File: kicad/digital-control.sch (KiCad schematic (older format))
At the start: 25 parts, among them J3 CONN_01X04, SW1 JS5208, U4 STM32F031G, U5 SSD1306-OLED-I2C, U6 MMA8652FC

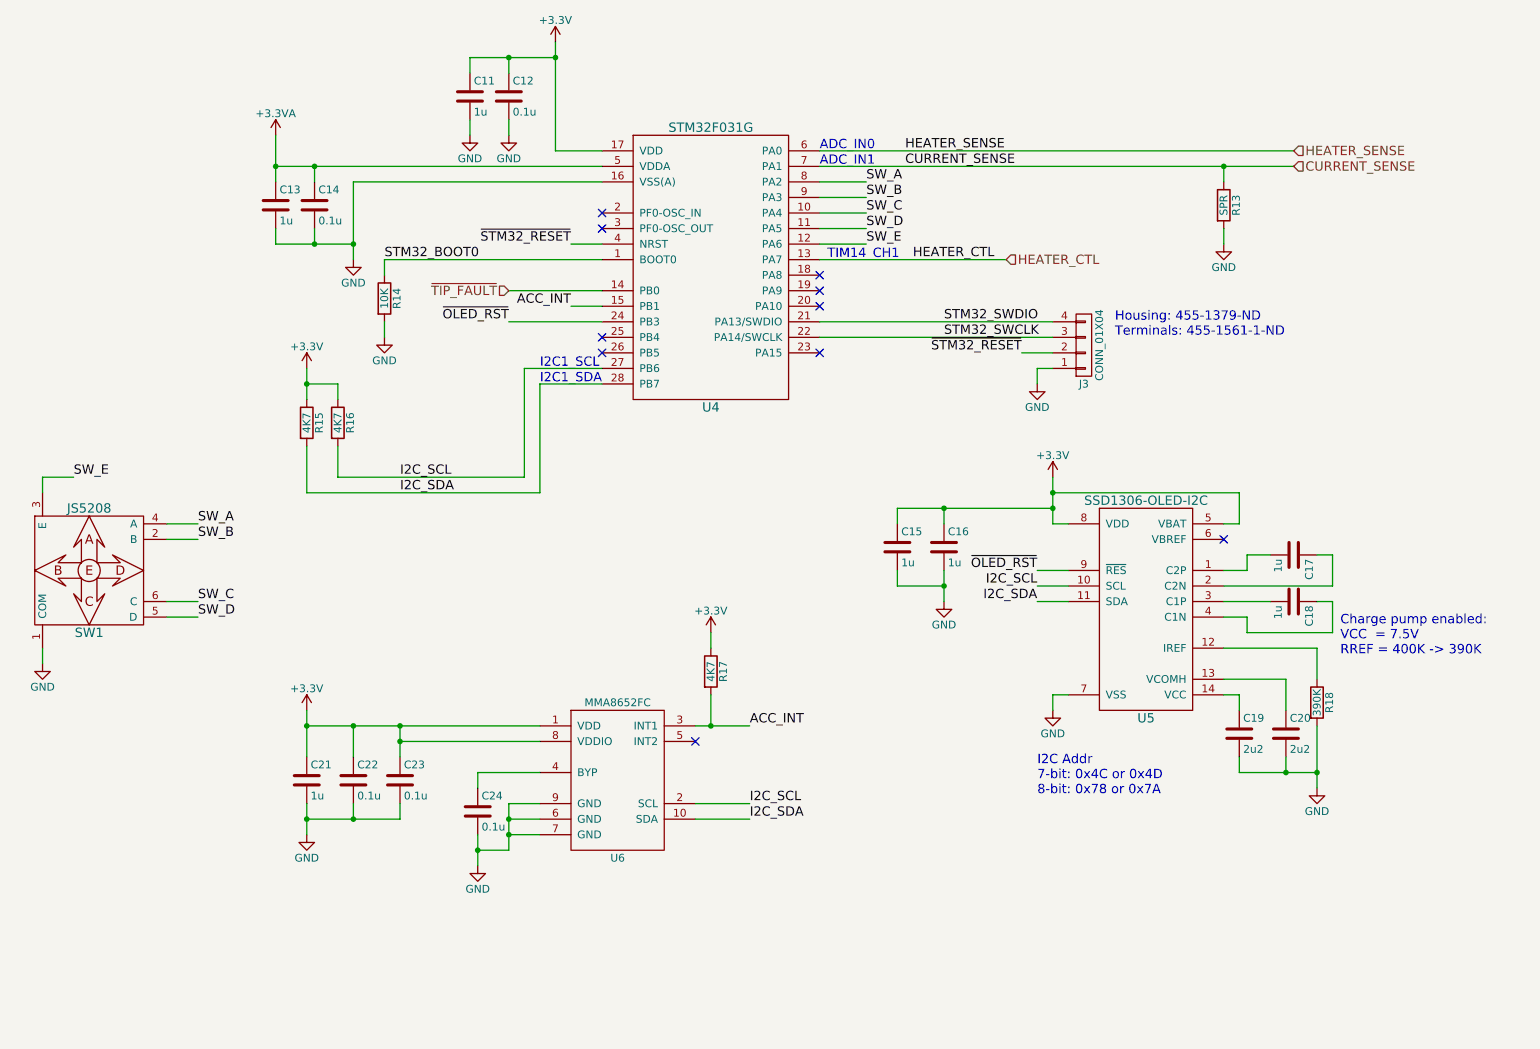
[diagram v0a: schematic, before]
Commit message: Added buzzer, fixed footprint errors, and updated silkscreen
The board is probably ready to be ordered
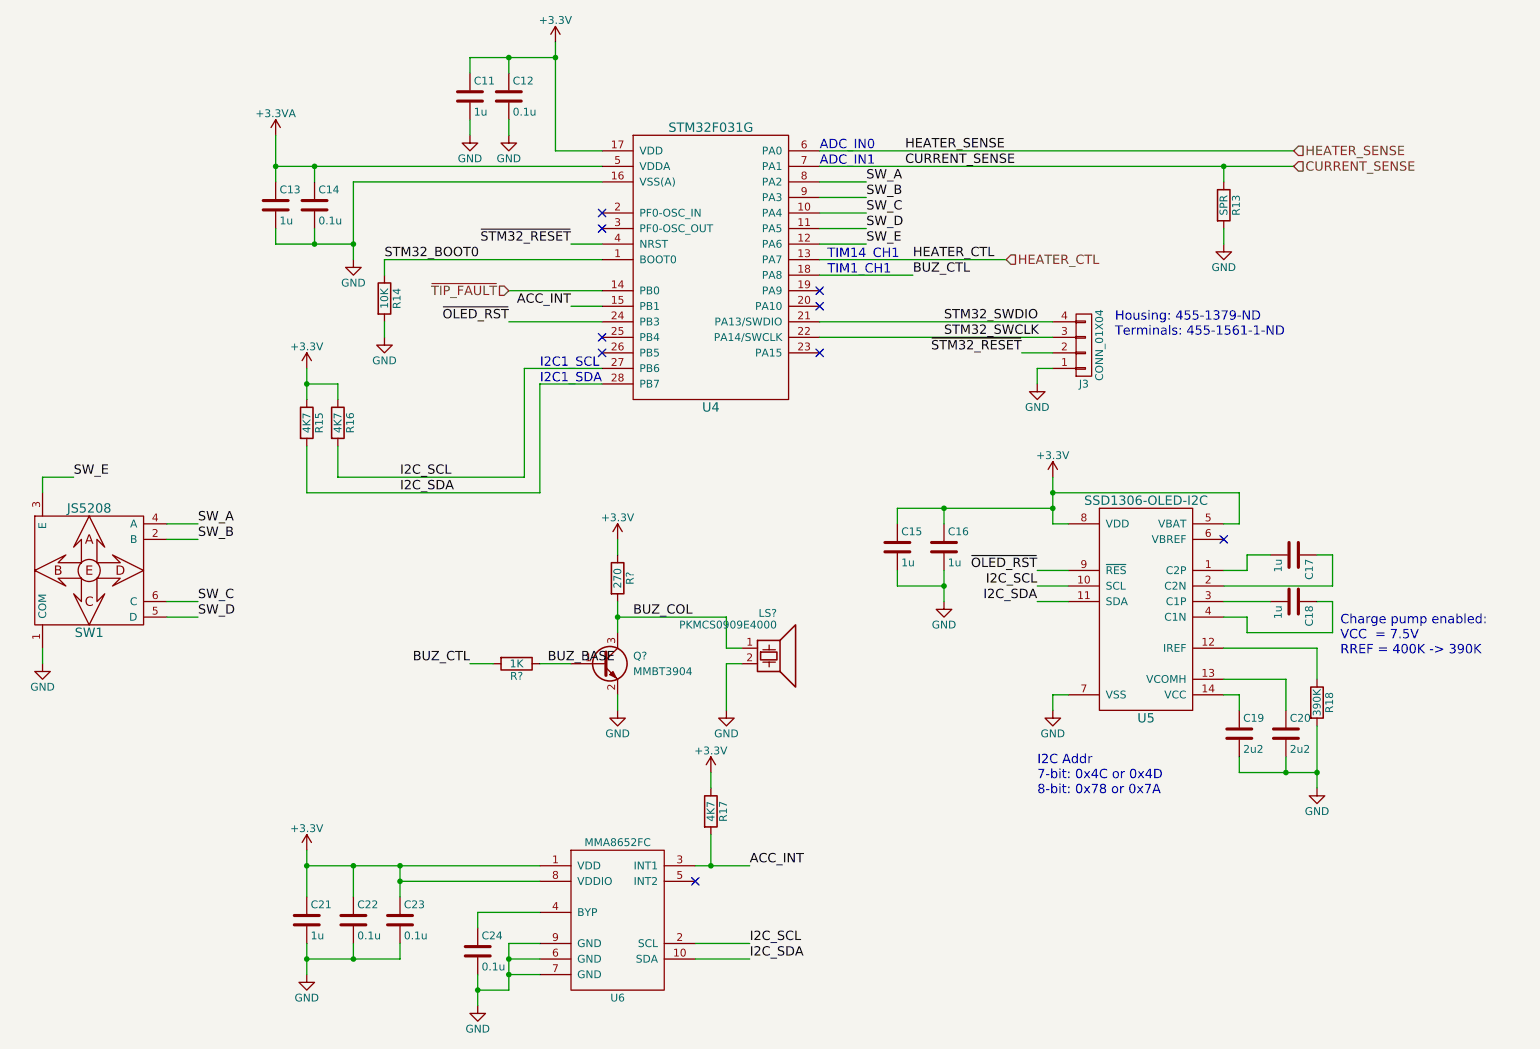
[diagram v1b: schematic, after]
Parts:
- added LS?: PKMCS0909E4000, rt-soldering-iron:Murata-PKMCS, symbol Speaker_Crystal
- added Q?: MMBT3904, TO_SOT_Packages_SMD:SOT-323_SC-70, symbol Q_NPN_BEC
- added R?: 270, Resistors_SMD:R_0402, symbol R
- added R?: 1K, Resistors_SMD:R_0402, symbol R
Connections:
- net +3V3: now also R?.1
- net GND: now also LS?.2, Q?.2 (E)
- net BUZ_CTL: now reaches U4.18 (PA8)
- net BUZ_CTL: now also R?.2
- new net BUZ_BASE: Q?.1 (B), R?.1
- new net BUZ_COL: LS?.1, Q?.3 (C), R?.2
- no-connect marks 10 -> 9
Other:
- note added: "TIM1_CH1"
- moved on the sheet: C21, C22, C23, C24, R17, U6

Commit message: Changed out the op amp and fixed oval holes for OSHPark
I don't think I'm going to go with OSHPark. It seems they can't
fabricate this thing.
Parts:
- gave numbers to parts that had none: 4
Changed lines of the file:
@@
 encoding utf-8
 Sheet 4 4
-Title ""
-Date ""
-Rev ""
-Comp ""
+Title "RT Soldering Iron"
+Date "2017-06-02"
+Rev "A"
+Comp "Kevin Cuzner"
 Comment1 ""
 Comment2 ""
@@
 $EndComp
 $Comp
-L +3.3V #PWR031
+L +3.3V #PWR33
 U 1 1 592BB6CC
 P 4600 1000
-F 0 "#PWR031" H 4600 850 50  0001 C CNN
+F 0 "#PWR33" H 4600 850 50  0001 C CNN
 F 1 "+3.3V" H 4600 1140 50  0000 C CNN
 F 2 "" H 4600 1000 50  0001 C CNN
@@
 $EndComp
 $Comp
-L GND #PWR032
+L GND #PWR38
 U 1 1 592BB766
 P 3300 2400
-F 0 "#PWR032" H 3300 2150 50  0001 C CNN
+F 0 "#PWR38" H 3300 2150 50  0001 C CNN
 F 1 "GND" H 3300 2250 50  0000 C CNN
 F 2 "" H 3300 2400 50  0001 C CNN
@@
 Connection ~ 4600 1100
 $Comp
-L GND #PWR033
+L GND #PWR36
 U 1 1 592BB8F3
 P 4300 1600
-F 0 "#PWR033" H 4300 1350 50  0001 C CNN
+F 0 "#PWR36" H 4300 1350 50  0001 C CNN
 F 1 "GND" H 4300 1450 50  0000 C CNN
 F 2 "" H 4300 1600 50  0001 C CNN
@@
 $EndComp
 $Comp
-L GND #PWR034
+L GND #PWR35
 U 1 1 592BB980
 P 4050 1600
-F 0 "#PWR034" H 4050 1350 50  0001 C CNN
+F 0 "#PWR35" H 4050 1350 50  0001 C CNN
 F 1 "GND" H 4050 1450 50  0000 C CNN
 F 2 "" H 4050 1600 50  0001 C CNN
@@
 	3500 2400 4900 2400
 $Comp
-L GND #PWR035
+L GND #PWR39
 U 1 1 592BBD79
 P 3500 2900
-F 0 "#PWR035" H 3500 2650 50  0001 C CNN
+F 0 "#PWR39" H 3500 2650 50  0001 C CNN
 F 1 "GND" H 3500 2750 50  0000 C CNN
 F 2 "" H 3500 2900 50  0001 C CNN
@@
 	2800 1800 4900 1800
 $Comp
-L +3.3VA #PWR036
+L +3.3VA #PWR34
 U 1 1 592C93D2
 P 2800 1600
-F 0 "#PWR036" H 2800 1450 50  0001 C CNN
+F 0 "#PWR34" H 2800 1450 50  0001 C CNN
 F 1 "+3.3VA" H 2800 1740 50  0000 C CNN
 F 2 "" H 2800 1600 50  0001 C CNN
@@
 	3000 3900 3000 3600
 $Comp
-L +3.3V #PWR037
+L +3.3V #PWR40
 U 1 1 592CB325
 P 3000 3100
-F 0 "#PWR037" H 3000 2950 50  0001 C CNN
+F 0 "#PWR40" H 3000 2950 50  0001 C CNN
 F 1 "+3.3V" H 3000 3240 50  0000 C CNN
 F 2 "" H 3000 3100 50  0001 C CNN
@@
 	7700 4600 7900 4600
 $Comp
-L GND #PWR038
+L GND #PWR48
 U 1 1 592CB60F
 P 7800 5300
-F 0 "#PWR038" H 7800 5050 50  0001 C CNN
+F 0 "#PWR48" H 7800 5050 50  0001 C CNN
 F 1 "GND" H 7800 5150 50  0000 C CNN
 F 2 "" H 7800 5300 50  0001 C CNN
@@
 Housing: 455-1379-ND\nTerminals: 455-1561-1-ND
 $Comp
-L +3.3V #PWR039
+L +3.3V #PWR42
 U 1 1 592CC5EE
 P 7800 3800
-F 0 "#PWR039" H 7800 3650 50  0001 C CNN
+F 0 "#PWR42" H 7800 3650 50  0001 C CNN
 F 1 "+3.3V" H 7800 3940 50  0000 C CNN
 F 2 "" H 7800 3800 50  0001 C CNN
@@
 	7800 4100 7900 4100
 $Comp
-L GND #PWR040
+L GND #PWR41
 U 1 1 592CC80A
 P 7700 3200
-F 0 "#PWR040" H 7700 2950 50  0001 C CNN
+F 0 "#PWR41" H 7700 2950 50  0001 C CNN
 F 1 "GND" H 7700 3050 50  0000 C CNN
 F 2 "" H 7700 3200 50  0001 C CNN
@@
 Connection ~ 3300 6300
 $Comp
-L GND #PWR041
+L GND #PWR52
 U 1 1 592CCD51
 P 3000 7000
-F 0 "#PWR041" H 3000 6750 50  0001 C CNN
+F 0 "#PWR52" H 3000 6750 50  0001 C CNN
 F 1 "GND" H 3000 6850 50  0000 C CNN
 F 2 "" H 3000 7000 50  0001 C CNN
@@
 $EndComp
 $Comp
-L +3.3V #PWR042
+L +3.3V #PWR51
 U 1 1 592CCDF7
 P 3000 6200
-F 0 "#PWR042" H 3000 6050 50  0001 C CNN
+F 0 "#PWR51" H 3000 6050 50  0001 C CNN
 F 1 "+3.3V" H 3000 6340 50  0000 C CNN
 F 2 "" H 3000 6200 50  0001 C CNN
@@
 	4100 6600 4100 6700
 $Comp
-L GND #PWR043
+L GND #PWR53
 U 1 1 592CD0B5
 P 4100 7200
-F 0 "#PWR043" H 4100 6950 50  0001 C CNN
+F 0 "#PWR53" H 4100 6950 50  0001 C CNN
 F 1 "GND" H 4100 7050 50  0000 C CNN
 F 2 "" H 4100 7200 50  0001 C CNN
@@
 	9500 4900 9500 5100
 $Comp
-L GND #PWR044
+L GND #PWR50
 U 1 1 592D0F0D
 P 9500 5800
-F 0 "#PWR044" H 9500 5550 50  0001 C CNN
+F 0 "#PWR50" H 9500 5550 50  0001 C CNN
 F 1 "GND" H 9500 5650 50  0000 C CNN
 F 2 "" H 9500 5800 50  0001 C CNN
@@
 Connection ~ 7100 4000
 $Comp
-L GND #PWR045
+L GND #PWR44
 U 1 1 592D28AB
 P 7100 4600
-F 0 "#PWR045" H 7100 4350 50  0001 C CNN
+F 0 "#PWR44" H 7100 4350 50  0001 C CNN
 F 1 "GND" H 7100 4450 50  0000 C CNN
 F 2 "" H 7100 4600 50  0001 C CNN
@@
 Connection ~ 8900 1800
 $Comp
-L GND #PWR046
+L GND #PWR37
 U 1 1 592D683B
 P 8900 2300
-F 0 "#PWR046" H 8900 2050 50  0001 C CNN
+F 0 "#PWR37" H 8900 2050 50  0001 C CNN
 F 1 "GND" H 8900 2150 50  0000 C CNN
 F 2 "" H 8900 2300 50  0001 C CNN
@@
 Connection ~ 5600 6300
 $Comp
-L +3.3V #PWR047
+L +3.3V #PWR49
 U 1 1 592D92EB
 P 5600 5700
-F 0 "#PWR047" H 5600 5550 50  0001 C CNN
+F 0 "#PWR49" H 5600 5550 50  0001 C CNN
 F 1 "+3.3V" H 5600 5840 50  0000 C CNN
 F 2 "" H 5600 5700 50  0001 C CNN
@@
 $EndComp
 $Comp
-L GND #PWR048
+L GND #PWR45
 U 1 1 592E2DAB
 P 1300 5000
-F 0 "#PWR048" H 1300 4750 50  0001 C CNN
+F 0 "#PWR45" H 1300 4750 50  0001 C CNN
 F 1 "GND" H 1300 4850 50  0000 C CNN
 F 2 "" H 1300 5000 50  0001 C CNN
@@
 	6600 1900 6300 1900
 $Comp
-L Speaker_Crystal LS?
+L Speaker_Crystal LS1
 U 1 1 592F94D2
 P 6000 4900
-F 0 "LS?" H 6025 5125 50  0000 R CNN
+F 0 "LS1" H 6025 5125 50  0000 R CNN
 F 1 "PKMCS0909E4000" H 6025 5050 50  0000 R CNN
 F 2 "rt-soldering-iron:Murata-PKMCS" H 5965 4850 50  0001 C CNN
@@
 $EndComp
 $Comp
-L Q_NPN_BEC Q?
+L Q_NPN_BEC Q3
 U 1 1 592F9D98
 P 4900 5000
-F 0 "Q?" H 5100 5050 50  0000 L CNN
+F 0 "Q3" H 5100 5050 50  0000 L CNN
 F 1 "MMBT3904" H 5100 4950 50  0000 L CNN
 F 2 "TO_SOT_Packages_SMD:SOT-323_SC-70" H 5100 5100 50  0001 C CNN
@@
 $EndComp
 $Comp
-L GND #PWR?
+L GND #PWR46
 U 1 1 592FA0EB
 P 5000 5300
-F 0 "#PWR?" H 5000 5050 50  0001 C CNN
+F 0 "#PWR46" H 5000 5050 50  0001 C CNN
 F 1 "GND" H 5000 5150 50  0000 C CNN
 F 2 "" H 5000 5300 50  0001 C CNN
@@
 $EndComp
 $Comp
-L R R?
+L R R19
 U 1 1 592FA1C8
 P 5000 4450
-F 0 "R?" V 5080 4450 50  0000 C CNN
+F 0 "R19" V 5080 4450 50  0000 C CNN
 F 1 "270" V 5000 4450 50  0000 C CNN
 F 2 "Resistors_SMD:R_0402" V 4930 4450 50  0001 C CNN
@@
 $EndComp
 $Comp
-L +3.3V #PWR?
+L +3.3V #PWR43
 U 1 1 592FA2D6
 P 5000 4200
-F 0 "#PWR?" H 5000 4050 50  0001 C CNN
+F 0 "#PWR43" H 5000 4050 50  0001 C CNN
 F 1 "+3.3V" H 5000 4340 50  0000 C CNN
 F 2 "" H 5000 4200 50  0001 C CNN
@@
 	5000 4200 5000 4300
 $Comp
-L GND #PWR?
+L GND #PWR47
 U 1 1 592FAF19
 P 5700 5300
-F 0 "#PWR?" H 5700 5050 50  0001 C CNN
+F 0 "#PWR47" H 5700 5050 50  0001 C CNN
 F 1 "GND" H 5700 5150 50  0000 C CNN
 F 2 "" H 5700 5300 50  0001 C CNN
@@
 Connection ~ 5000 4700
 $Comp
-L R R?
+L R R20
 U 1 1 592FB329
 P 4350 5000
-F 0 "R?" V 4430 5000 50  0000 C CNN
+F 0 "R20" V 4430 5000 50  0000 C CNN
 F 1 "1K" V 4350 5000 50  0000 C CNN
 F 2 "Resistors_SMD:R_0402" V 4280 5000 50  0001 C CNN

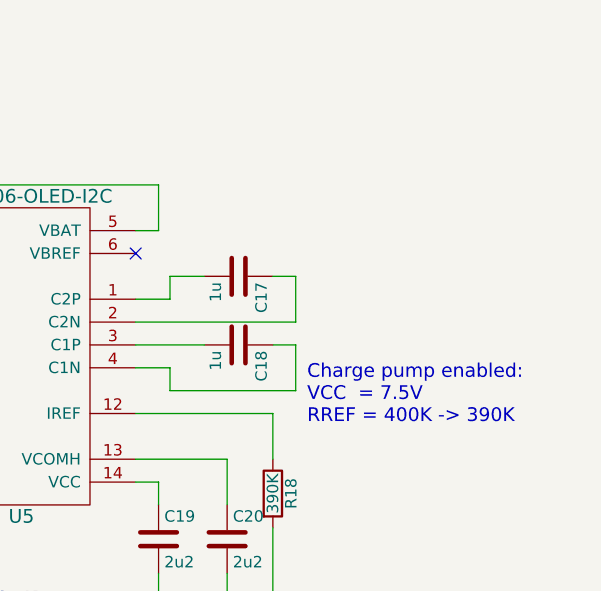
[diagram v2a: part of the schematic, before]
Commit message: Fixed schematic to use USLetter paper
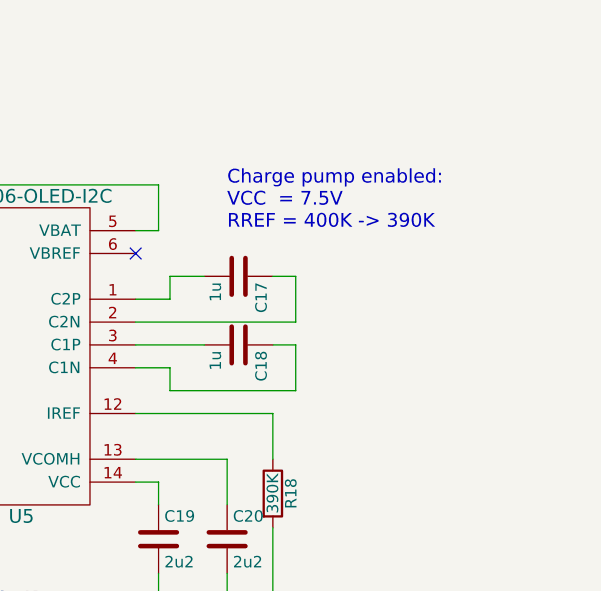
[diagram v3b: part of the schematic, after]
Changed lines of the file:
@@
 EELAYER 25 0
 EELAYER END
-$Descr A4 11693 8268
+$Descr USLetter 11000 8500
 encoding utf-8
 Sheet 4 4
@@
 Text Notes 4500 3200 0    60   ~ 0
 I2C1_SDA
-Text Notes 9650 4950 0    60   ~ 0
+Text Notes 9300 4100 0    60   ~ 0
 Charge pump enabled:\nVCC  = 7.5V\nRREF = 400K -> 390K
 $Comp

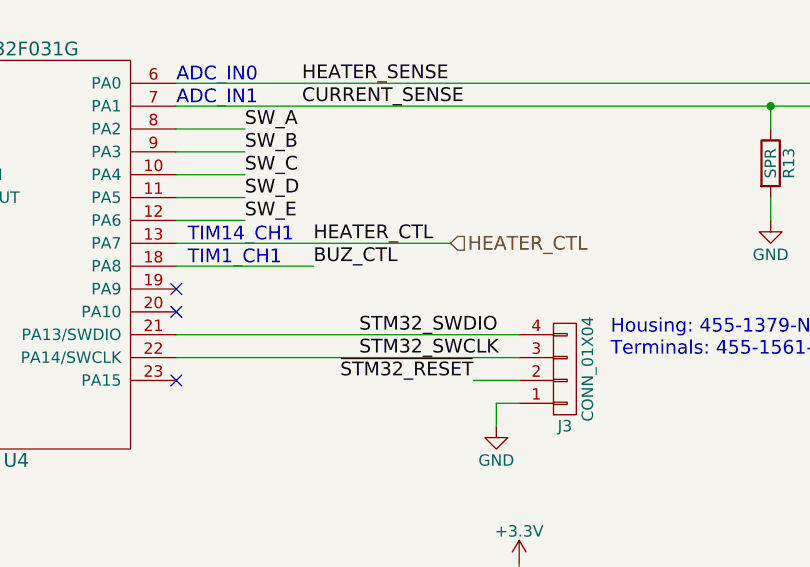
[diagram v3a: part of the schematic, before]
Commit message: Started second revision, added a comparator and eFuse
The comparator has no hysteresis in its current configuration, so that
will need to be fixed.
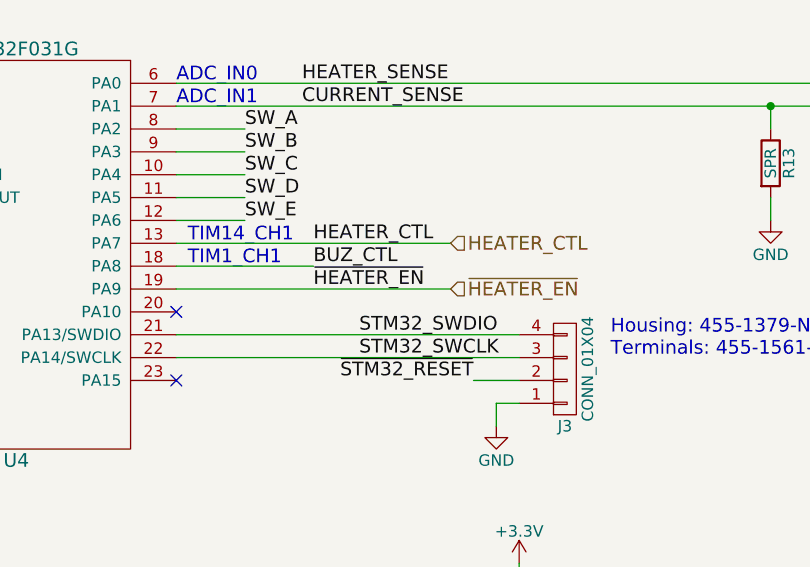
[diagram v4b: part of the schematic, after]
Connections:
- net ~HEATER_EN: now reaches U4.19 (PA9)
- no-connect marks 9 -> 8
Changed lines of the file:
@@
 NoConn ~ 4900 3000
 NoConn ~ 6300 2700
-NoConn ~ 6300 2600
 $Comp
 L JS5208 SW1
@@
 Text Label 5100 4700 0    60   ~ 0
 BUZ_COL
+Text HLabel 7500 2600 2    60   Input ~ 0
+~HEATER_EN
+Wire Wire Line
+	7500 2600 6300 2600
+Text Label 6900 2600 0    60   ~ 0
+~HEATER_EN
 $EndSCHEMATC
